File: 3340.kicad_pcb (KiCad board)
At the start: 2 copper layers, 221.2 x 128.5 mm, 180 parts, among them J1 Conn_01x17, J10 FM1, J11 Conn_01x17, J12 V/OCT2, J13 PULSE2, J14 SAW2, J15 TRI2, J16 SINE2, J17 SYNC2, J18 Conn_01x17, J19 PWM2, J2 Conn_01x17, J20 FM2, J3 V/OCT1, J4 PULSE1, J5 SAW1, J6 TRI1, J7 SINE1, J8 SYNC1, J9 PWM1, Q1 2N3904, Q2 2N3906, Q3 2N3904, Q4 2N3906, Q5 2N3904, Q6 2N3904, SW2 DPDT_OOO, U1 TL072, U2 TL074, U3 CEM3340, U4 TL072, U5 CEM3340, U6 TL074

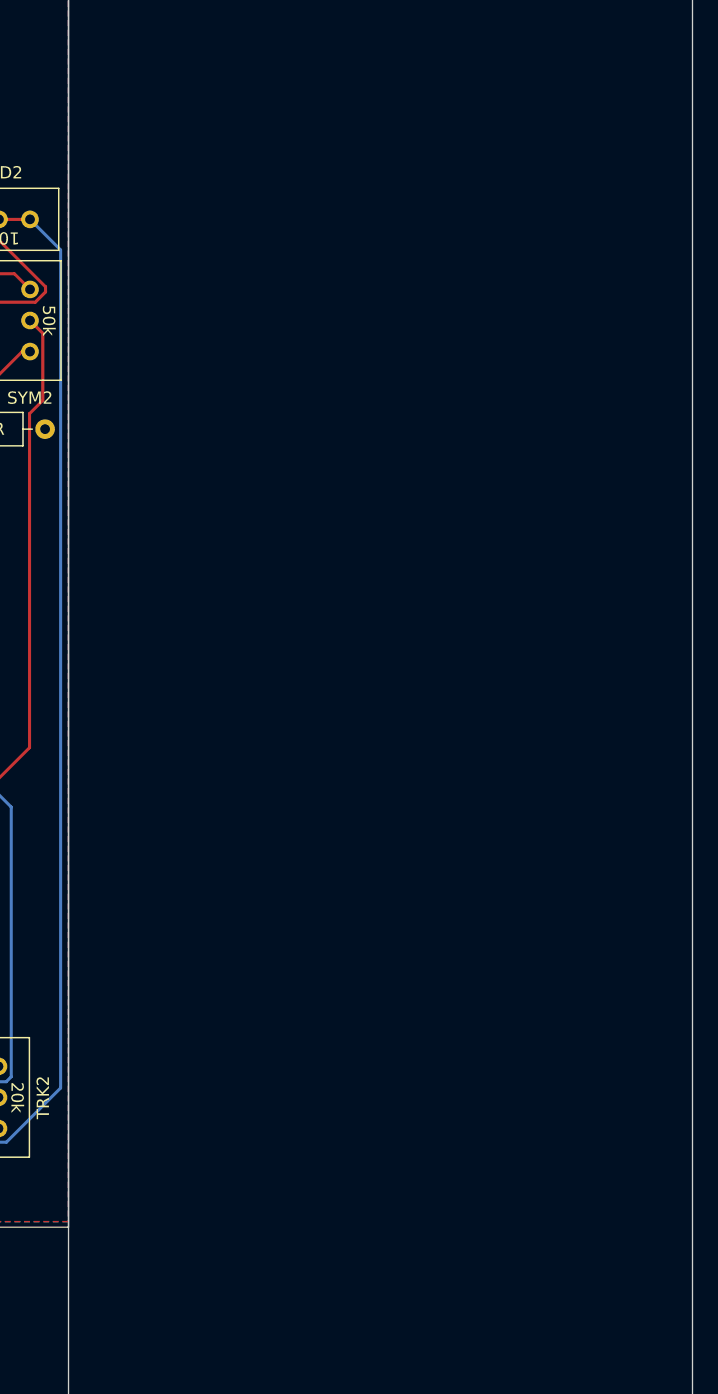
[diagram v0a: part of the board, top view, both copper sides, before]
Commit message: Add panel holes
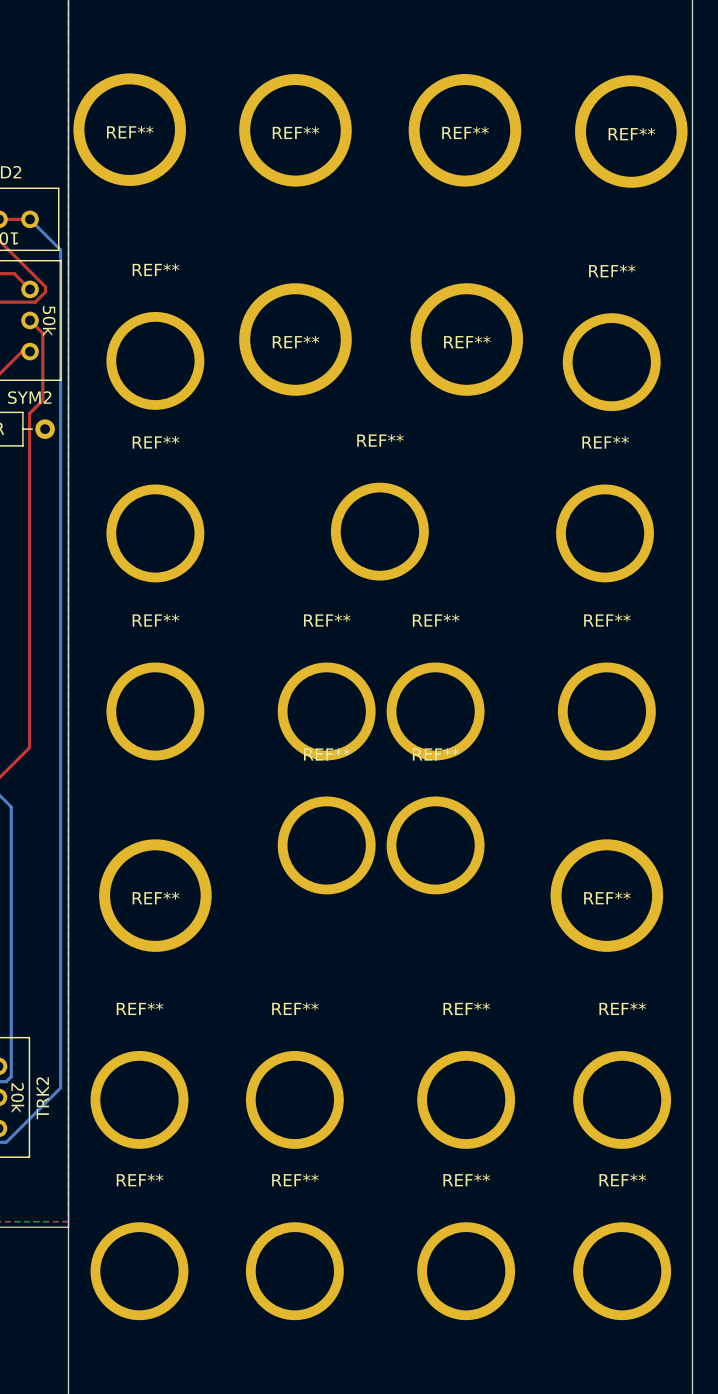
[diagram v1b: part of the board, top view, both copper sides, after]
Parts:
- added REF**: MountingHole_7.4mm_M7_Pad_VeryNarrow, MountingHole:MountingHole_7.4mm_M7_Pad_VeryNarrow, F.Cu at (187.9, 29.5)
- added REF**: MountingHole_6.4mm_M6_Pad_VeryNarrow, MountingHole:MountingHole_6.4mm_M6_Pad_VeryNarrow, F.Cu at (188.7, 122.8)
- added REF**: MountingHole_6.4mm_M6_Pad_VeryNarrow, MountingHole:MountingHole_6.4mm_M6_Pad_VeryNarrow, F.Cu at (228.2, 108.8)
- added REF**: MountingHole_6.4mm_M6_Pad_VeryNarrow, MountingHole:MountingHole_6.4mm_M6_Pad_VeryNarrow, F.Cu at (212.9, 77.0)
- added REF**: MountingHole_6.4mm_M6_Pad_VeryNarrow, MountingHole:MountingHole_6.4mm_M6_Pad_VeryNarrow, F.Cu at (190.0, 62.5)
- added REF**: MountingHole_7.4mm_M7_Pad_VeryNarrow, MountingHole:MountingHole_7.4mm_M7_Pad_VeryNarrow, F.Cu at (226.9, 92.1)
- added REF**: MountingHole_6.4mm_M6_Pad_VeryNarrow, MountingHole:MountingHole_6.4mm_M6_Pad_VeryNarrow, F.Cu at (190.0, 77.0)
- added REF**: MountingHole_6.4mm_M6_Pad_VeryNarrow, MountingHole:MountingHole_6.4mm_M6_Pad_VeryNarrow, F.Cu at (201.4, 108.8)
- added REF**: MountingHole_7.4mm_M7_Pad_VeryNarrow, MountingHole:MountingHole_7.4mm_M7_Pad_VeryNarrow, F.Cu at (215.4, 46.6)
- added REF**: MountingHole_7.4mm_M7_Pad_VeryNarrow, MountingHole:MountingHole_7.4mm_M7_Pad_VeryNarrow, F.Cu at (201.4, 29.6)
- added REF**: MountingHole_6.4mm_M6_Pad_VeryNarrow, MountingHole:MountingHole_6.4mm_M6_Pad_VeryNarrow, F.Cu at (226.9, 77.0)
- added REF**: MountingHole_6.4mm_M6_Pad_VeryNarrow, MountingHole:MountingHole_6.4mm_M6_Pad_VeryNarrow, F.Cu at (201.4, 122.8)
- added REF**: MountingHole_6.4mm_M6_Pad_VeryNarrow, MountingHole:MountingHole_6.4mm_M6_Pad_VeryNarrow, F.Cu at (226.8, 62.5)
- added REF**: MountingHole_7.4mm_M7_Pad_VeryNarrow, MountingHole:MountingHole_7.4mm_M7_Pad_VeryNarrow, F.Cu at (201.4, 46.6)
- added REF**: MountingHole_7.4mm_M7_Pad_VeryNarrow, MountingHole:MountingHole_7.4mm_M7_Pad_VeryNarrow, F.Cu at (190.0, 92.1)
- added REF**: MountingHole_6.4mm_M6_Pad_VeryNarrow, MountingHole:MountingHole_6.4mm_M6_Pad_VeryNarrow, F.Cu at (212.9, 88.0)
- added REF**: MountingHole_6.4mm_M6_Pad_VeryNarrow, MountingHole:MountingHole_6.4mm_M6_Pad_VeryNarrow, F.Cu at (215.4, 108.8)
- added REF**: MountingHole_6.4mm_M6_Pad_VeryNarrow, MountingHole:MountingHole_6.4mm_M6_Pad_VeryNarrow, F.Cu at (188.7, 108.8)
- added REF**: MountingHole_7.4mm_M7_Pad_VeryNarrow, MountingHole:MountingHole_7.4mm_M7_Pad_VeryNarrow, F.Cu at (228.9, 29.6)
- added REF**: MountingHole_6.4mm_M6_Pad_VeryNarrow, MountingHole:MountingHole_6.4mm_M6_Pad_VeryNarrow, F.Cu at (204.0, 88.0)
- added REF**: MountingHole_6.4mm_M6_Pad_VeryNarrow, MountingHole:MountingHole_6.4mm_M6_Pad_VeryNarrow, F.Cu at (228.2, 122.8)
- added REF**: MountingHole_7.4mm_M7_Pad_VeryNarrow, MountingHole:MountingHole_7.4mm_M7_Pad_VeryNarrow, F.Cu at (215.3, 29.6)
- added REF**: MountingHole_6.4mm_M6_Pad_VeryNarrow, MountingHole:MountingHole_6.4mm_M6_Pad_VeryNarrow, F.Cu at (208.3, 62.4)
- added REF**: MountingHole_6.4mm_M6_Pad_VeryNarrow, MountingHole:MountingHole_6.4mm_M6_Pad_VeryNarrow, F.Cu at (227.3, 48.5)
- added REF**: MountingHole_6.4mm_M6_Pad_VeryNarrow, MountingHole:MountingHole_6.4mm_M6_Pad_VeryNarrow, F.Cu at (190.0, 48.4)
- added REF**: MountingHole_6.4mm_M6_Pad_VeryNarrow, MountingHole:MountingHole_6.4mm_M6_Pad_VeryNarrow, F.Cu at (215.4, 122.8)
- added REF**: MountingHole_6.4mm_M6_Pad_VeryNarrow, MountingHole:MountingHole_6.4mm_M6_Pad_VeryNarrow, F.Cu at (204.0, 77.0)

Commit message: Fill testing
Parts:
- renumbered REF** to REF**1, REF** to REF**10, REF** to REF**11, REF** to REF**12, REF** to REF**13, REF** to REF**14, REF** to REF**15, REF** to REF**16, REF** to REF**17, REF** to REF**18, REF** to REF**19, REF** to REF**2, REF** to REF**20, REF** to REF**21, REF** to REF**22, REF** to REF**23, REF** to REF**24, REF** to REF**25, REF** to REF**26, REF** to REF**27, REF** to REF**28, REF** to REF**29, REF** to REF**3, REF** to REF**30, REF** to REF**31, REF** to REF**4, REF** to REF**5, REF** to REF**6, REF** to REF**7, REF** to REF**8, REF** to REF**9

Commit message: Fix switch footprints
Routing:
- net Net-(C19-Pad1): track 40.7 -> 39.0 mm
- net /PWM1: track 112.9 -> 111.5 mm
- net +12V: track 360.2 -> 359.0 mm
- net Net-(C8-Pad1): track 16.8 -> 15.8 mm
- net Net-(COARSE1-Pad2): track 32.2 -> 33.0 mm
- net /12v: track 95.8 -> 95.1 mm
- net /PWM2: track 80.9 -> 80.2 mm
- net /PULSEOUT2: track 69.7 -> 69.0 mm
- net Net-(C12-Pad2): track 6.80 -> 6.14 mm
- net Net-(R59-Pad1): track 4.23 -> 3.58 mm
- net /SINE2: track 137.3 -> 136.7 mm
- net /PW_IN1: track 48.1 -> 47.5 mm
- net Net-(R10-Pad1): track 7.39 -> 6.75 mm
- net Net-(C21-Pad1): track 7.91 -> 7.28 mm
- net Net-(R53-Pad2): track 6.38 -> 5.76 mm
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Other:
- board text added: "d&j dual 3340 rev1.0 by laughing blue panel board"
- board text added: "d&j dual 3340 rev1.0 left board"
- board text added: "d&j dual 3340 rev1.0 right board"

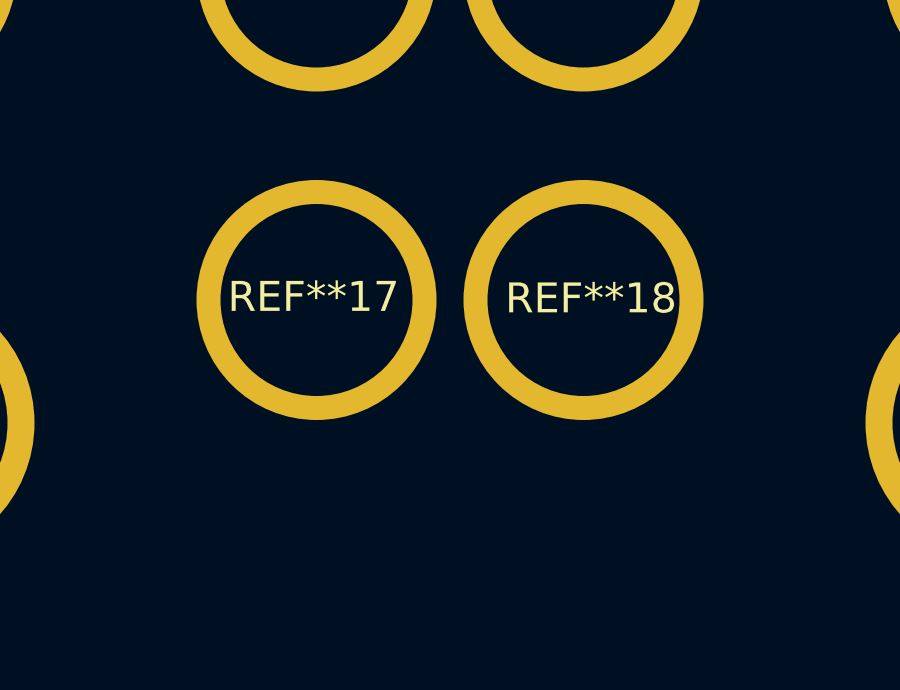
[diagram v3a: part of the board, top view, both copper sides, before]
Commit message: Add some panel hole nets
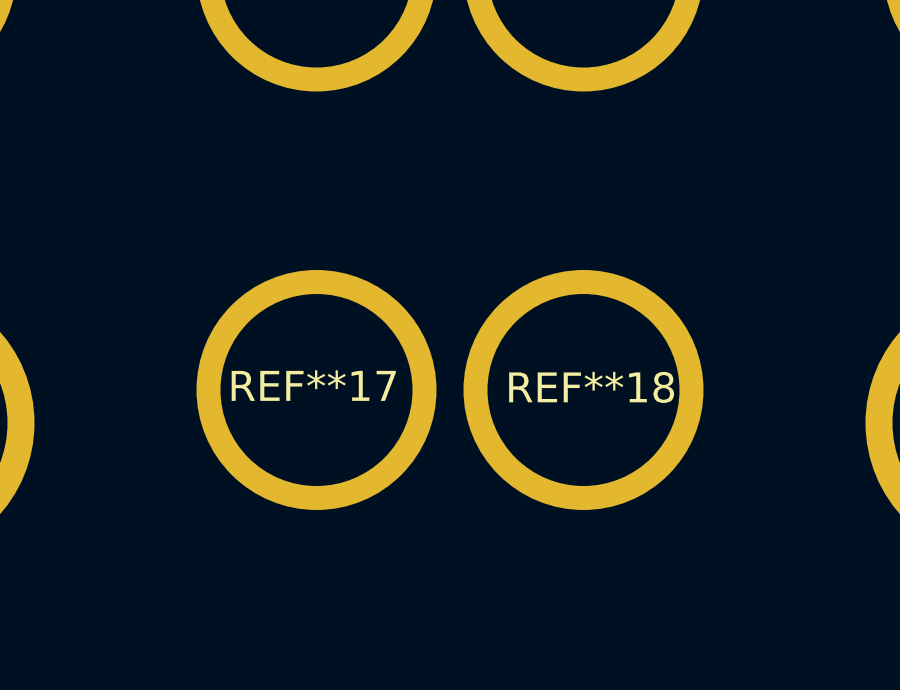
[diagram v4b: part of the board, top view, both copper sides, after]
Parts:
- moved REF**17 3.00 mm to (204.0, 91.0)
- moved REF**18 3.00 mm to (212.9, 91.0)
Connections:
- REF**1 pad 1: (no net) -> GND
- REF**10 pad 1: (no net) -> GND
- REF**11 pad 1: (no net) -> GND
- REF**12 pad 1: (no net) -> GND
- REF**13 pad 1: (no net) -> GND
- REF**14 pad 1: (no net) -> GND
- REF**2 pad 1: (no net) -> GND
- REF**3 pad 1: (no net) -> GND
- REF**4 pad 1: (no net) -> GND
- REF**5 pad 1: (no net) -> GND
- REF**6 pad 1: (no net) -> GND
- REF**7 pad 1: (no net) -> GND
- REF**8 pad 1: (no net) -> GND
